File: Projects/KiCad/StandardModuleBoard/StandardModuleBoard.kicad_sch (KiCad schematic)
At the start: 9 parts, among them J1 Conn_01x04_Male, J2 Conn_01x04_Female, U1 MCP2562-E-P, U2 NUCLEO-F303K8

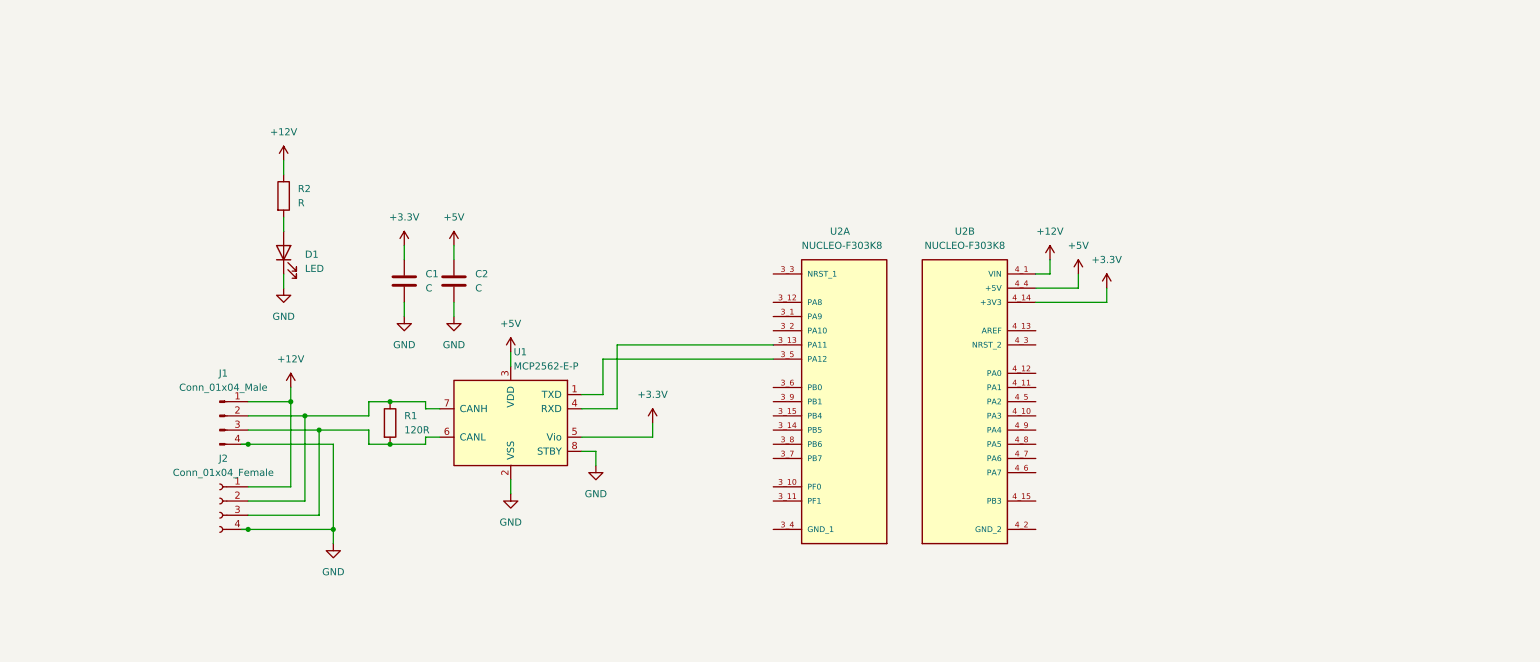
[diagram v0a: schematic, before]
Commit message: 標準モジュールの回路図を修正 SPIのプルアップ抵抗難しい。抵抗値は基板製造時にオシロで見るしかない
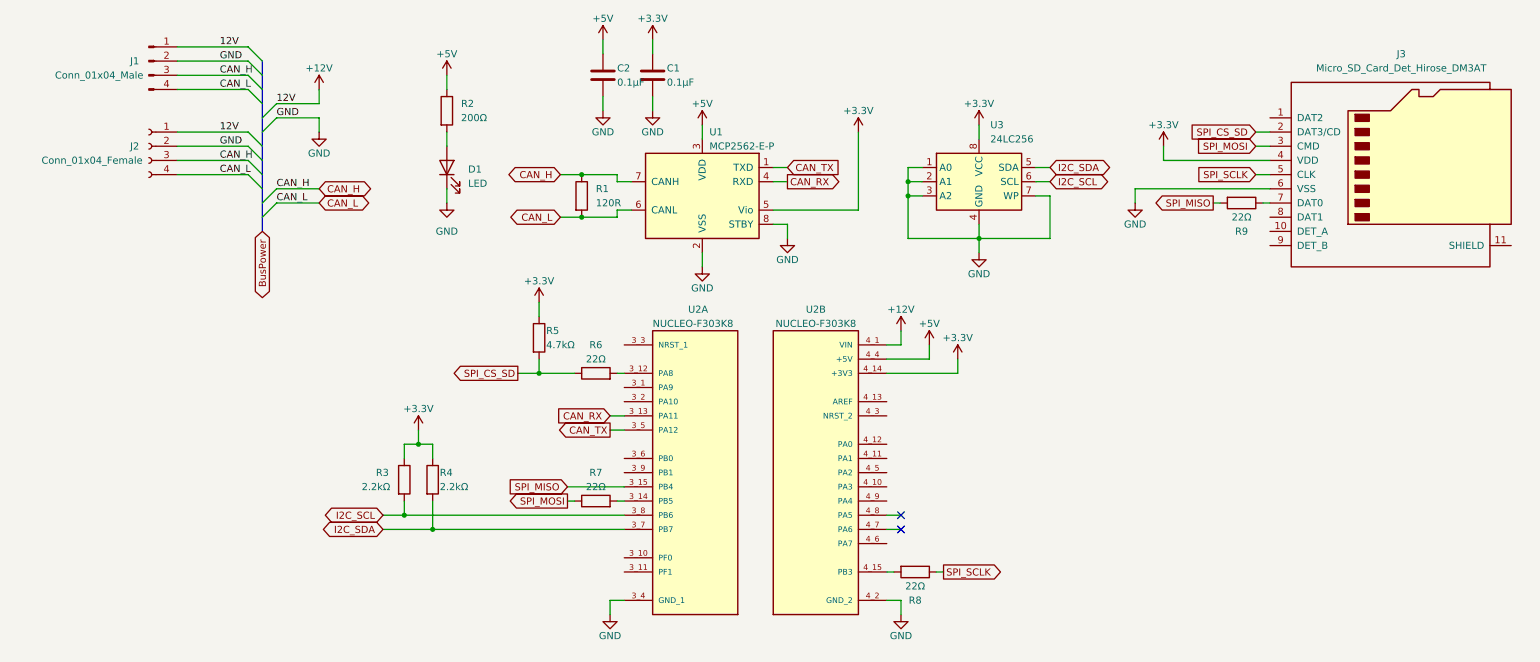
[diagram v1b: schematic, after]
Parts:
- added J3: Micro_SD_Card_Det_Hirose_DM3AT, symbol Connector:Micro_SD_Card_Det_Hirose_DM3AT
- added R3, R4: 2.2kΩ, symbol Device:R
- added R5: 4.7kΩ, symbol Device:R
- added R6, R7, R8, R9: 22Ω, symbol Device:R
- added U3: 24LC256, symbol Memory_EEPROM:24LC256
- C1, C2: value C -> 0.1μF
- R2: value R -> 200Ω
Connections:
- net +12V: no longer R2.1
- net +3.3V: now also J3.4 (VDD), R3.1, R4.1, R5.1, U3.8 (VCC)
- net +5V: now also R2.1
- net GND: now also J1.2 (Pin_2), J2.2 (Pin_2), U2.3_4 (GND_1), U2.4_2 (GND_2), J3.6 (VSS), U3.1 (A0), U3.2 (A1), U3.3 (A2), U3.4 (GND), U3.7 (WP); no longer J1.4 (Pin_4), J2.4 (Pin_4)
- net CAN_TX: now reaches U1.1 (TXD), U2.3_5 (PA12)
- net CAN_RX: now reaches U1.4 (RXD), U2.3_13 (PA11)
- net CAN_H: now reaches J1.3 (Pin_3), J2.3 (Pin_3)
- net CAN_H: now also R1.1, U1.7 (CANH); no longer R1.2, U1.6 (CANL)
- net at U2.4_15 (PB3): now also R8.2
- net at U2.3_12 (PA8): now also R6.2
- net at U2.3_14 (PB5): now also R7.2
- net SPI_MISO: now reaches U2.3_15 (PB4)
- net SPI_MISO: now also R9.2
- net I2C_SDA: now reaches U2.3_7 (PB7)
- net I2C_SDA: now also R4.2, U3.5 (SDA)
- net I2C_SCL: now reaches U2.3_8 (PB6)
- net I2C_SCL: now also R3.2, U3.6 (SCL)
- new net: J3.7 (DAT0), R9.1
- new net CAN_L: J1.4 (Pin_4), J2.4 (Pin_4), R1.2, U1.6 (CANL)
- new net SPI_CS_SD: J3.2 (DAT3/CD), R5.2, R6.1
- new net SPI_MOSI: J3.3 (CMD), R7.1
- new net SPI_SCLK: J3.5 (CLK), R8.1
- no-connect marks 0 -> 2
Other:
- moved on the sheet: C1, C2, D1, J1, J2, R1, R2, U1, U2A, U2B

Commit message: 標準モジュール基板の回路図を修正
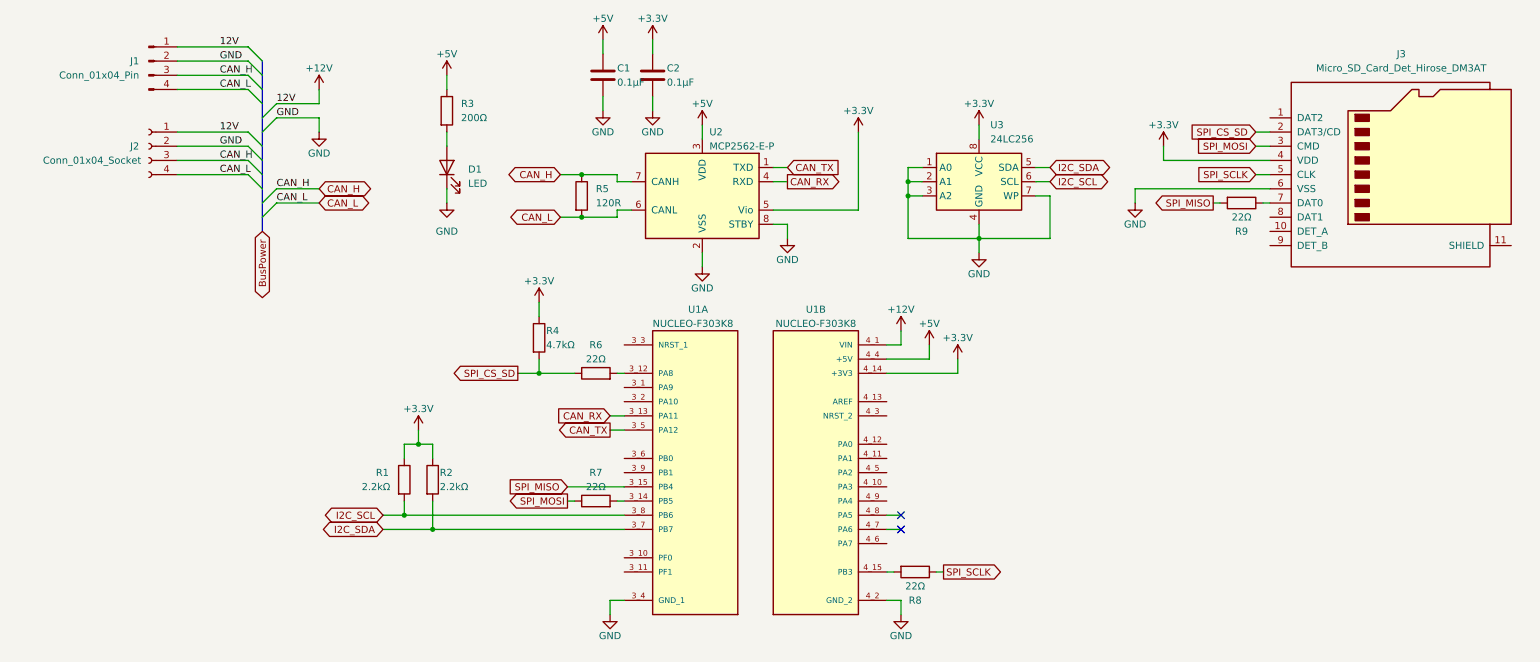
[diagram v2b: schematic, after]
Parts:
- removed J1: Conn_01x04_Male, Connector_PinHeader_1.27mm:PinHeader_1x04_P1.27mm_Vertical, symbol Connector:Conn_01x04_Male
- removed J2: Conn_01x04_Female, Connector_PinSocket_1.27mm:PinSocket_1x04_P1.27mm_Vertical, symbol Connector:Conn_01x04_Female
- added J1: Conn_01x04_Pin, symbol Connector:Conn_01x04_Pin
- added J2: Conn_01x04_Socket, symbol Connector:Conn_01x04_Socket
- C1: renamed from C2; footprint Capacitor_SMD:C_0402_1005Metric_Pad0.74x0.62mm_HandSolder -> (none)
- C2: renamed from C1; footprint Capacitor_SMD:C_0402_1005Metric_Pad0.74x0.62mm_HandSolder -> (none)
- D1: footprint LED_SMD:LED_0603_1608Metric_Pad1.05x0.95mm_HandSolder -> (none)
- R3: renamed from R2; footprint Resistor_SMD:R_1206_3216Metric_Pad1.30x1.75mm_HandSolder -> (none)
- R5: renamed from R1; footprint Resistor_SMD:R_0603_1608Metric_Pad0.98x0.95mm_HandSolder -> (none)
- renumbered R3 to R1, R4 to R2, R5 to R4, U2 to U1, U1 to U2
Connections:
- net +12V: now also J1.1 (Pin_1), J2.1 (Pin_1)
- net CAN_H: now also J1.3 (Pin_3), J2.3 (Pin_3)
- net CAN_L: now also J1.4 (Pin_4), J2.4 (Pin_4)
- net GND: now also J1.2 (Pin_2), J2.2 (Pin_2)

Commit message: 標準モジュール基板のボード図を修正
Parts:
- C1, C2: footprint (none) -> Capacitor_SMD:C_0805_2012Metric_Pad1.18x1.45mm_HandSolder
- J1: footprint (none) -> Connector_PinHeader_1.27mm:PinHeader_1x04_P1.27mm_Vertical
- J2: footprint (none) -> Connector_PinSocket_1.27mm:PinSocket_1x04_P1.27mm_Vertical
- J3: footprint (none) -> Connector_Card:microSD_HC_Hirose_DM3AT-SF-PEJM5
- R1, R2, R4, R6, R7, R8, R9: footprint (none) -> Resistor_SMD:R_1206_3216Metric_Pad1.30x1.75mm_HandSolder
- R5: value 120R -> 120R1/4W; footprint (none) -> Resistor_SMD:R_1206_3216Metric_Pad1.30x1.75mm_HandSolder
- U3: footprint (none) -> Package_DIP:DIP-8_W7.62mm
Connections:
- no-connect marks 2 -> 22
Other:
- moved on the sheet: D1, J1, J2, R3, R9

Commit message: 標準モジュールにパイロットランプを追加
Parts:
- D1: footprint (none) -> LED_SMD:LED_1206_3216Metric_Pad1.42x1.75mm_HandSolder
- R1, R2, R4, R5, R6, R7, R8, R9: footprint Resistor_SMD:R_1206_3216Metric_Pad1.30x1.75mm_HandSolder -> Resistor_SMD:R_0805_2012Metric_Pad1.20x1.40mm_HandSolder
- R3: value 200Ω -> 2kΩ; footprint (none) -> Resistor_SMD:R_0805_2012Metric_Pad1.20x1.40mm_HandSolder
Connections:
- net +12V: now also R3.1
- net +5V: no longer R3.1
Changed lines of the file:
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@@
       (effects (font (size 1.27 1.27)) (justify left))
     )
-    (property "Footprint" "Resistor_SMD:R_1206_3216Metric_Pad1.30x1.75mm_HandSolder" (at 104.902 73.66 90)
+    (property "Footprint" "Resistor_SMD:R_0805_2012Metric_Pad1.20x1.40mm_HandSolder" (at 104.902 73.66 90)
       (effects (font (size 1.27 1.27)) hide)
     )
@@
       (effects (font (size 1.27 1.27)))
     )
-    (property "Footprint" "Resistor_SMD:R_1206_3216Metric_Pad1.30x1.75mm_HandSolder" (at 229.87 47.752 90)
+    (property "Footprint" "Resistor_SMD:R_0805_2012Metric_Pad1.20x1.40mm_HandSolder" (at 229.87 47.752 90)
       (effects (font (size 1.27 1.27)) hide)
     )
@@
       (effects (font (size 1.27 1.27)))
     )
-    (property "Footprint" "Resistor_SMD:R_1206_3216Metric_Pad1.30x1.75mm_HandSolder" (at 116.84 81.788 90)
+    (property "Footprint" "Resistor_SMD:R_0805_2012Metric_Pad1.20x1.40mm_HandSolder" (at 116.84 81.788 90)
       (effects (font (size 1.27 1.27)) hide)
     )
@@
         (path "/ea1ed597-7cd3-4340-902e-bdce8f2d7a62"
           (reference "#PWR05") (unit 1)
+        )
+      )
+    )
+  )
+  (symbol (lib_id "power:+12V") (at 74.93 26.67 0) (unit 1)
+    (in_bom yes) (on_board yes) (dnp no) (fields_autoplaced)
+    (property "Reference" "#PWR04" (at 74.93 30.48 0)
+      (effects (font (size 1.27 1.27)) hide)
+    )
+    (property "Value" "+12V" (at 74.93 22.86 0)
+      (effects (font (size 1.27 1.27)))
+    )
+    (property "Footprint" "" (at 74.93 26.67 0)
+      (effects (font (size 1.27 1.27)) hide)
+    )
+    (property "Datasheet" "" (at 74.93 26.67 0)
+      (effects (font (size 1.27 1.27)) hide)
+    )
+    (pin "1")
+    (instances
+      (project "StandardModuleBoard"
+        (path "/ea1ed597-7cd3-4340-902e-bdce8f2d7a62"
+          (reference "#PWR04") (unit 1)
         )
       )
@@
       (effects (font (size 1.27 1.27)) (justify left))
     )
-    (property "Footprint" "Resistor_SMD:R_1206_3216Metric_Pad1.30x1.75mm_HandSolder" (at 80.772 99.06 90)
+    (property "Footprint" "Resistor_SMD:R_0805_2012Metric_Pad1.20x1.40mm_HandSolder" (at 80.772 99.06 90)
       (effects (font (size 1.27 1.27)) hide)
     )
@@
       (effects (font (size 1.27 1.27)) (justify left))
     )
-    (property "Value" "200Ω" (at 77.47 34.2899 0)
-      (effects (font (size 1.27 1.27)) (justify left))
-    )
-    (property "Footprint" "" (at 73.152 33.02 90)
+    (property "Value" "2kΩ" (at 77.47 34.2899 0)
+      (effects (font (size 1.27 1.27)) (justify left))
+    )
+    (property "Footprint" "Resistor_SMD:R_0805_2012Metric_Pad1.20x1.40mm_HandSolder" (at 73.152 33.02 90)
       (effects (font (size 1.27 1.27)) hide)
     )
@@
       (effects (font (size 1.27 1.27)) (justify right))
     )
-    (property "Footprint" "" (at 74.93 43.18 0)
+    (property "Footprint" "LED_SMD:LED_1206_3216Metric_Pad1.42x1.75mm_HandSolder" (at 74.93 43.18 0)
       (effects (font (size 1.27 1.27)) hide)
     )
@@
       (effects (font (size 1.27 1.27)))
     )
-    (property "Footprint" "Resistor_SMD:R_1206_3216Metric_Pad1.30x1.75mm_HandSolder" (at 173.99 113.792 90)
+    (property "Footprint" "Resistor_SMD:R_0805_2012Metric_Pad1.20x1.40mm_HandSolder" (at 173.99 113.792 90)
       (effects (font (size 1.27 1.27)) hide)
     )
@@
       (effects (font (size 1.27 1.27)))
     )
-    (property "Footprint" "Resistor_SMD:R_1206_3216Metric_Pad1.30x1.75mm_HandSolder" (at 116.84 104.648 90)
+    (property "Footprint" "Resistor_SMD:R_0805_2012Metric_Pad1.20x1.40mm_HandSolder" (at 116.84 104.648 90)
       (effects (font (size 1.27 1.27)) hide)
     )
@@
     )
   )
-  (symbol (lib_id "power:+5V") (at 74.93 26.67 0) (unit 1)
-    (in_bom yes) (on_board yes) (dnp no) (fields_autoplaced)
-    (property "Reference" "#PWR04" (at 74.93 30.48 0)
-      (effects (font (size 1.27 1.27)) hide)
-    )
-    (property "Value" "+5V" (at 74.93 22.86 0)
-      (effects (font (size 1.27 1.27)))
-    )
-    (property "Footprint" "" (at 74.93 26.67 0)
-      (effects (font (size 1.27 1.27)) hide)
-    )
-    (property "Datasheet" "" (at 74.93 26.67 0)
-      (effects (font (size 1.27 1.27)) hide)
-    )
-    (pin "1")
-    (instances
-      (project "StandardModuleBoard"
-        (path "/ea1ed597-7cd3-4340-902e-bdce8f2d7a62"
-          (reference "#PWR04") (unit 1)
-        )
-      )
-    )
-  )
   (symbol (lib_id "power:GND") (at 118.11 33.02 0) (unit 1)
     (in_bom yes) (on_board yes) (dnp no) (fields_autoplaced)
@@
       (effects (font (size 1.27 1.27)) (justify left))
     )
-    (property "Footprint" "Resistor_SMD:R_1206_3216Metric_Pad1.30x1.75mm_HandSolder" (at 85.852 99.06 90)
+    (property "Footprint" "Resistor_SMD:R_0805_2012Metric_Pad1.20x1.40mm_HandSolder" (at 85.852 99.06 90)
       (effects (font (size 1.27 1.27)) hide)
     )
@@
       (effects (font (size 1.27 1.27)) (justify left))
     )
-    (property "Footprint" "Resistor_SMD:R_1206_3216Metric_Pad1.30x1.75mm_HandSolder" (at 112.522 48.26 90)
-      (effects (font (size 1.27 1.27)) hide)
-    )
+    (property "Footprint" "Resistor_SMD:R_0805_2012Metric_Pad1.20x1.40mm_HandSolder" (at 112.522 48.26 90)
+      (effects (font (size 1.27 1.27)) hide)
+    )
